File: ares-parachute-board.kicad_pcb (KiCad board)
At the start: 2 copper layers, 57 x 88 mm, 133 parts, among them J1 Conn_01x16_Female, J2 Conn_01x16_Female, J3 Conn_01x02_Male

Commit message: rename project
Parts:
- added U1: STM32F103CBTx, Package_QFP:LQFP-48_7x7mm_P0.5mm, F.Cu at (5.17, 5.17)
- added U2: LIS2DH, Package_LGA:LGA-14_2x2mm_P0.35mm_LayoutBorder3x4y, F.Cu at (1.32, 12.7)
- added U3: LIS2DH, Package_LGA:LGA-14_2x2mm_P0.35mm_LayoutBorder3x4y, F.Cu at (4.81, 12.7)

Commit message: re-annotate, component placement complete
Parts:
- added C10: 12.5p, Capacitor_SMD:C_0603_1608Metric, F.Cu at (189.6, 82.2)
- added C11: 100n, Capacitor_SMD:C_0603_1608Metric, F.Cu at (187.6, 67.8)
- added C12: 100n, Capacitor_SMD:C_0603_1608Metric, F.Cu at (197.0, 67.6)
- added C13: 100n, Capacitor_SMD:C_0603_1608Metric, F.Cu at (195.8, 78.6)
- added C14: 100n, Capacitor_SMD:C_0603_1608Metric, F.Cu at (185.6, 75.0)
- added C15: 4u7, Capacitor_SMD:C_0603_1608Metric, F.Cu at (187.0, 76.6)
- added C16: 100n, Capacitor_SMD:C_0603_1608Metric, F.Cu at (219.6, 83.0)
- added C17: 1F, asyd-parachute:SCMR18C105MRBA0, F.Cu at (196.0, 117.2)
- added C2: 1u, Capacitor_SMD:C_0603_1608Metric, F.Cu at (206.8, 62.6)
- added C3: 1u, Capacitor_SMD:C_0603_1608Metric, F.Cu at (200.0, 57.4)
- added C4: 10u, Capacitor_SMD:C_0603_1608Metric, F.Cu at (195.2, 61.6)
- added C5: 100n, Capacitor_SMD:C_0603_1608Metric, F.Cu at (196.8, 61.6)
- added C6: 47p, Capacitor_SMD:C_0603_1608Metric, F.Cu at (192.8, 61.8)
- added C7: 100n, Capacitor_SMD:C_0603_1608Metric, F.Cu at (205.0, 73.0)
- added C8: 12.5p, Capacitor_SMD:C_0603_1608Metric, F.Cu at (187.2, 82.2)
- added C9: 100n, Capacitor_SMD:C_0603_1608Metric, F.Cu at (204.2, 82.6)
- added J4: Conn_ARM_JTAG_SWD_10, Connector_PinHeader_1.27mm:PinHeader_2x05_P1.27mm_Vertical, F.Cu at (182.0, 67.8)
- added J5: Conn_01x03_Pin, Connector_PinHeader_2.54mm:PinHeader_1x03_P2.54mm_Horizontal, F.Cu at (226.2, 55.7)
- added J6: MPT 0.5/2-2.54, TerminalBlock_Phoenix:TerminalBlock_Phoenix_MPT-0,5-2-2.54_1x02_P2.54mm_Horizontal, F.Cu at (184.6, 101.1)
- added JP1: Jumper_3_Bridged12, Connector_PinHeader_2.54mm:PinHeader_1x03_P2.54mm_Horizontal, F.Cu at (191.6, 113.1)
- added LED1: RED, easyeda_exported:LED0805-R-RD, F.Cu at (199.4, 65.8)
- added LED2: RED, easyeda_exported:LED0805-R-RD, F.Cu at (214.2, 75.0)
- added LED3: YLW, easyeda_exported:LED0805-R-RD, F.Cu at (214.2, 72.4)
- added LED4: GRN, easyeda_exported:LED0805-R-RD, F.Cu at (214.2, 69.8)
- added R1: 33, Resistor_SMD:R_0603_1608Metric, F.Cu at (189.6, 61.8)
- added R10: 4k7, Resistor_SMD:R_0603_1608Metric, F.Cu at (217.2, 85.2)
- added R11: 4k7, Resistor_SMD:R_0603_1608Metric, F.Cu at (219.6, 87.4)
- added R12: 270, Resistor_SMD:R_0603_1608Metric, F.Cu at (210.4, 75.0)
- added R13: 270, Resistor_SMD:R_0603_1608Metric, F.Cu at (210.4, 72.4)
- added R14: 100, Resistor_SMD:R_0603_1608Metric, F.Cu at (210.4, 69.8)
- added R15: 100, Resistor_SMD:R_0603_1608Metric, F.Cu at (194.6, 106.8)
- added R2: 33, Resistor_SMD:R_0603_1608Metric, F.Cu at (191.2, 61.8)
- added R3: 270, Resistor_SMD:R_0603_1608Metric, F.Cu at (201.4, 65.2)
- added R4: 56k, Resistor_SMD:R_0603_1608Metric, F.Cu at (198.2, 57.4)
- added R5: 5.1k, Resistor_SMD:R_0603_1608Metric, F.Cu at (195.8, 55.0)
- added R6: 5.1k, Resistor_SMD:R_0603_1608Metric, F.Cu at (195.8, 58.2)
- added R7: 4k7, Resistor_SMD:R_0603_1608Metric, F.Cu at (201.8, 85.0)
- added R8: 4k7, Resistor_SMD:R_0603_1608Metric, F.Cu at (204.2, 87.2)
- added R9: 0, Resistor_SMD:R_0603_1608Metric, F.Cu at (193.4, 79.6)
- added U3: SR05-ES, Package_TO_SOT_SMD:SOT-143, F.Cu at (182.8, 56.8)
- added U4: W25Q128JVSIQTR, easyeda_exported:SOIC-8_L5.3-W5.3-P1.27-LS8.0-BL, F.Cu at (201.4, 73.0)
- added U6: STM32F103CBTx, Package_QFP:LQFP-48_7x7mm_P0.5mm, F.Cu at (192.4, 72.4)
- added U7: LIS2DW12TR, easyeda_exported:LGA-12_L2.0-W2.0-P0.50-BL, F.Cu at (219.7, 85.2)
- added USB1: TYPE-C16PIN, easyeda_exported:USB-C-SMD_TYPE-C16PIN, F.Cu at (189.8, 57.1)
- added X1: CSTNE8M00G520000R0, easyeda_exported:OSC-SMD_3P-L3.2-W1.3-P1.20, F.Cu at (191.6, 79.6)
- added X2: Q13FC1350000400, easyeda_exported:FC-135R_L3.2-W1.5, F.Cu at (188.4, 79.4)
- C1: value 1F -> 47p; footprint asyd-parachute:SCMR18C105MRBA0 -> Capacitor_SMD:C_0603_1608Metric
- U1: value STM32F103CBTx -> XC6206P332MR; footprint Package_QFP:LQFP-48_7x7mm_P0.5mm -> easyeda_exported:SOT-23-3_L2.9-W1.6-P1.90-LS2.8-BR
- U2: value LIS2DH -> AP2552W6-7; footprint Package_LGA:LGA-14_2x2mm_P0.35mm_LayoutBorder3x4y -> easyeda_exported:SOT-26_L3.0-W1.6-P0.95-LS2.8-BL
- U5: renamed from U3; value LIS2DH -> LIS2DW12TR; footprint Package_LGA:LGA-14_2x2mm_P0.35mm_LayoutBorder3x4y -> easyeda_exported:LGA-12_L2.0-W2.0-P0.50-BL
- moved U5 212.1 mm to (204.2, 85.0)
- moved U1 206.9 mm to (204.0, 62.4), turned to 90 degrees
- moved U2 204.8 mm to (200.4, 60.8), turned to -90 degrees
- moved C1 53.7 mm to (188.0, 61.8)
- moved REF** 27.8 mm to (184.6, 130.2)
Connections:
- net P0 renamed /DET+
- net P1 renamed /DET-
- net P13 renamed /PB9
- net P14 renamed /PB12
- net P15 renamed /PB13
- net P16 renamed /PB14
- net P19 renamed /PB15
- net P2 renamed /PB0
- net P20 renamed /PA3
- net P8 renamed /PB5
- net P9 renamed /PB8
- net btn_a renamed /PB1
- net btn_b renamed /PB2
- C1 pad 1: +3V3 -> /USB_D+
- J1 pad 1: +3V3 -> +3.3V
- J1 pad 3: MOT- -> +5V
- J2 pad 1: +3V3 -> +3.3V
- J2 pad 3: MOT- -> +5V
- U1 pad 1: unconnected-(U1-VBAT-Pad1) -> GND
- U1 pad 2: unconnected-(U1-PC13-Pad2) -> +5V
- U1 pad 3: unconnected-(U1-PC14-Pad3) -> +3.3V
- U2 pad 1: unconnected-(U2-SCL/SPC-Pad1) -> VBUS
- U2 pad 2: unconnected-(U2-SDA/SDI-Pad2) -> GND
- U2 pad 3: unconnected-(U2-SDO-Pad3) -> GND
- U2 pad 4: unconnected-(U2-~{CS}-Pad4) -> Net-(U2-~{FAULT})
- U2 pad 5: unconnected-(U2-INT2-Pad5) -> Net-(U2-ILIM)
- U2 pad 6: unconnected-(U2-INT1-Pad6) -> +5V
- U5 pad 1: unconnected-(U3-SCL/SPC-Pad1) -> /I2C1_SCL
- U5 pad 10: Net-(U3-GND-Pad10) -> +3.3V
- U5 pad 11: Net-(U3-GND-Pad10) -> unconnected-(U5-INT2-Pad11)
- U5 pad 12: Net-(U3-GND-Pad10) -> unconnected-(U5-INT1-Pad12)
- U5 pad 2: unconnected-(U3-SDA/SDI-Pad2) -> +3.3V
- U5 pad 3: unconnected-(U3-SDO-Pad3) -> GND
- U5 pad 4: unconnected-(U3-~{CS}-Pad4) -> /I2C1_SDA
- U5 pad 6: unconnected-(U3-INT1-Pad6) -> GND
- U5 pad 7: unconnected-(U3-Vdd_IO-Pad7) -> GND
- U5 pad 8: unconnected-(U3-Vdd-Pad8) -> GND
- U5 pad 9: Net-(U3-GND-Pad10) -> +3.3V
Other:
- board text added: "ARES Parachute Board PROTO1 (c) 2024 Hochschule Luzern, Technik & Architektur"
- board text added: "PA0"
- board text added: "PA1"
- board text added: "PA2"
- board text added: "Power Stuff"
- board text added: "X"
- board text added: "Y"
- board text added: "Z"
- board text added: "up"
- board text removed: "ASYD Parachute Board v1.3, SMD CONNECTOR (c) 2023 Hochschule Luzern, Technik & Architektur"

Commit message: about to try some stuff
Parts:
- removed J2: Conn_01x16_Female, Connector_PinHeader_2.54mm:PinHeader_1x16_P2.54mm_Vertical
- moved LED2 14.5 mm to (226.0, 66.5)
- moved R12 14.5 mm to (222.2, 66.5)
- moved LED3 12.3 mm to (226.0, 68.9)
- moved R13 12.3 mm to (222.2, 68.9)
- moved U4 12.3 mm to (213.2, 69.6)
- moved C7 12.3 mm to (216.8, 69.6)
- moved R14 11.9 mm to (222.2, 71.3)
- moved LED4 11.9 mm to (226.0, 71.3)
- moved C6 5.63 mm to (187.4, 63.4)
- moved J4 5.49 mm to (181.8, 62.4)
- moved C1 4.49 mm to (192.2, 63.4)
- moved R6 3.41 mm to (196.0, 54.8), turned to -90 degrees
- moved R5 3.01 mm to (196.0, 58.0), turned to 90 degrees
- moved R2 2.72 mm to (189.0, 63.4)
- moved R1 1.89 mm to (190.6, 63.4)
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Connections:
- net Net-(USB1-DN1) renamed /d-
- net Net-(USB1-DP1) renamed /d+
- J5 pad 1: /USART1_TX -> /USART1_RX
- J5 pad 2: /USART1_RX -> /USART1_TX
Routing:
- net +3.3V: track 0.00 -> 143.1 mm, vias 0 -> 4
- net +5V: track 0.00 -> 66.5 mm
- net /I2C1_SDA: track 0.00 -> 47.1 mm, vias 0 -> 2
- net /I2C2_SDA: track 0.00 -> 45.6 mm, vias 0 -> 4
- net /I2C1_SCL: track 0.00 -> 43.1 mm, vias 0 -> 2
- net /USART1_RX: track 0.00 -> 40.1 mm, vias 0 -> 2
- net /PB8: track 0.00 -> 39.9 mm, vias 0 -> 1
- net /PB5: track 0.00 -> 39.4 mm, vias 0 -> 2
- net /PB9: track 0.00 -> 39.4 mm, vias 0 -> 1
- net /USART1_TX: track 0.00 -> 38.6 mm, vias 0 -> 2
- net /I2C2_SCL: track 0.00 -> 37.1 mm, vias 0 -> 4
- net /RED: track 0.00 -> 37.1 mm, vias 0 -> 4
- net /YLW: track 0.00 -> 34.7 mm, vias 0 -> 4
- net VBUS: track 0.00 -> 34.0 mm, vias 0 -> 2
- net /GRN: track 0.00 -> 32.0 mm, vias 0 -> 4
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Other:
- outline, holes or cut-outs redrawn

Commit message: layout done
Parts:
- removed the   at (228.6, 133.3)
- added  : , asyd-parachute:my_pin, F.Cu at (205.4, 124.8)
- added  : , asyd-parachute:my_pin, F.Cu at (207.9, 129.8)
- added  : , asyd-parachute:my_pin, F.Cu at (207.9, 132.4)
- added  : , asyd-parachute:my_pin, F.Cu at (205.4, 112.1)
- added  : , asyd-parachute:my_pin, F.Cu at (210.5, 127.3)
- added  : , asyd-parachute:my_pin, F.Cu at (207.9, 117.1)
- added  : , asyd-parachute:my_pin, F.Cu at (207.9, 119.7)
- added  : , asyd-parachute:my_pin, F.Cu at (205.4, 109.5)
- added  : , asyd-parachute:my_pin, F.Cu at (207.9, 109.5)
- added  : , asyd-parachute:my_pin, F.Cu at (210.5, 119.7)
- added  : , asyd-parachute:my_pin, F.Cu at (207.9, 137.5)
- added  : , asyd-parachute:my_pin, F.Cu at (205.4, 122.2)
- added  : , asyd-parachute:my_pin, F.Cu at (207.9, 112.1)
- added  : , asyd-parachute:my_pin, F.Cu at (210.5, 117.1)
- added  : , asyd-parachute:my_pin, F.Cu at (210.5, 114.6)
- added  : , asyd-parachute:my_pin, F.Cu at (205.4, 129.8)
- added  : , asyd-parachute:my_pin, F.Cu at (205.4, 127.3)
- added  : , asyd-parachute:my_pin, F.Cu at (210.5, 122.2)
- added  : , asyd-parachute:my_pin, F.Cu at (210.5, 132.4)
- added  : , asyd-parachute:my_pin, F.Cu at (210.5, 107.0)
- added  : , asyd-parachute:my_pin, F.Cu at (205.4, 107.0)
- added  : , asyd-parachute:my_pin, F.Cu at (210.5, 109.5)
- added  : , asyd-parachute:my_pin, F.Cu at (210.5, 124.8)
- added  : , asyd-parachute:my_pin, F.Cu at (205.4, 134.9)
- added  : , asyd-parachute:my_pin, F.Cu at (210.5, 104.4)
- added  : , asyd-parachute:my_pin, F.Cu at (205.4, 114.6)
- added  : , asyd-parachute:my_pin, F.Cu at (207.9, 122.2)
- added  : , asyd-parachute:my_pin, F.Cu at (205.4, 119.7)
- added  : , asyd-parachute:my_pin, F.Cu at (207.9, 124.8)
- added  : , asyd-parachute:my_pin, F.Cu at (210.5, 137.5)
- added  : , asyd-parachute:my_pin, F.Cu at (205.4, 104.4)
- added  : , asyd-parachute:my_pin, F.Cu at (205.4, 132.4)
- added  : , asyd-parachute:my_pin, F.Cu at (210.5, 129.8)
- added  : , asyd-parachute:my_pin, F.Cu at (205.4, 117.1)
- added  : , asyd-parachute:my_pin, F.Cu at (207.9, 107.0)
- added  : , asyd-parachute:my_pin, F.Cu at (210.5, 112.1)
- added  : , asyd-parachute:my_pin, F.Cu at (205.4, 137.5)
- added  : , asyd-parachute:my_pin, F.Cu at (207.9, 104.4)
- added  : , asyd-parachute:my_pin, F.Cu at (207.9, 134.9)
- added  : , asyd-parachute:my_pin, F.Cu at (207.9, 114.6)
- added  : , asyd-parachute:my_pin, F.Cu at (210.5, 134.9)
- added  : , asyd-parachute:my_pin, F.Cu at (207.9, 127.3)
- added REF**: MountingHole_2.2mm_M2, MountingHole:MountingHole_2.2mm_M2, F.Cu at (182.3, 97.4)
- added REF**: MountingHole_2.2mm_M2, MountingHole:MountingHole_2.2mm_M2, F.Cu at (234.8, 75.2)
- added REF**: MountingHole_2.2mm_M2, MountingHole:MountingHole_2.2mm_M2, F.Cu at (234.2, 137.4)
- added REF**: MountingHole_2.2mm_M2, MountingHole:MountingHole_2.2mm_M2, F.Cu at (190.0, 97.1)
- added REF**: MountingHole_2.2mm_M2, MountingHole:MountingHole_2.2mm_M2, F.Cu at (234.7, 83.6)
- added REF**: MountingHole_2.2mm_M2, MountingHole:MountingHole_2.2mm_M2, F.Cu at (184.6, 83.5)
- added REF**: MountingHole_2.2mm_M2, MountingHole:MountingHole_2.2mm_M2, F.Cu at (202.6, 137.4)
- moved R15 9.90 mm to (190.7, 115.9), turned to 0 degrees
- moved J1 6.35 mm to (195.6, 98.0), turned to 90 degrees
- moved   6.27 mm to (225.7, 134.9)
- moved   6.27 mm to (225.7, 137.5)
- moved   6.27 mm to (225.7, 109.5)
- moved   6.27 mm to (225.7, 114.6)
- moved   6.27 mm to (225.7, 117.1)
- moved   6.27 mm to (225.7, 104.4)
- moved   6.27 mm to (225.7, 119.7)
- moved   6.27 mm to (225.7, 122.2)
- moved   6.27 mm to (225.7, 127.3)
- moved   6.27 mm to (225.7, 107.0)
- moved   6.27 mm to (225.7, 112.1)
- moved   6.27 mm to (225.7, 124.8)
- moved   6.27 mm to (225.7, 129.8)
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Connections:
- J1 pad 1: +3.3V -> +5V
- J1 pad 10: /PB8 -> /PB1
- J1 pad 11: /PB9 -> /PB2
- J1 pad 12: /PB12 -> /PB15
- J1 pad 13: /PB13 -> /PB14
- J1 pad 14: /PB14 -> /PB13
- J1 pad 15: /PB15 -> /PB12
- J1 pad 16: /PA3 -> unconnected-(J1-Pin_16-Pad16)
- J1 pad 2: GND -> +3.3V
- J1 pad 3: +5V -> GND
- J1 pad 6: /PB0 -> /PB5
- J1 pad 7: /PB1 -> /PB8
- J1 pad 8: /PB2 -> /PB9
- J1 pad 9: /PB5 -> /PB0
- JP1 pad 1: +5V -> Net-(JP1-A)
- JP1 pad 3: Net-(JP1-B) -> +5V
- R15 pad 2: Net-(JP1-B) -> Net-(JP1-A)
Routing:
- net /PB12: track 1.78 -> 59.2 mm, vias 1 -> 5
- net /PB13: track 2.15 -> 57.4 mm, vias 1 -> 5
- net /PB14: track 2.07 -> 55.7 mm, vias 1 -> 5
- net /PB15: track 1.21 -> 52.8 mm, vias 1 -> 5
- net /PB2: track 0.00 -> 42.7 mm, vias 0 -> 2
- net /PB1: track 0.00 -> 41.3 mm, vias 0 -> 2
- net /PB0: track 0.00 -> 40.0 mm, vias 0 -> 2
- net /PB9: track 39.4 -> 56.5 mm, vias 1 -> 2
- net /PB8: track 39.9 -> 55.4 mm, vias 1 -> 2
- net /PB5: track 39.4 -> 53.9 mm
- net +5V: track 66.5 -> 60.0 mm, vias 0 -> 2
- net +3.3V: track 143.1 -> 149.5 mm, vias 4 -> 6
- net Net-(JP1-B): track 3.20 -> 0.00 mm
- net GND: track 13.6 -> 16.6 mm, vias 23 -> 32
- net Net-(JP1-A): track 0.00 -> 2.80 mm
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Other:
- outline, holes or cut-outs redrawn
- board text added: "3V3"
- board text added: "5V"
- board text added: "DET+"
- board text added: "DET-"
- board text added: "GND"
- board text added: "I2C1"
- board text added: "I2C2"
- board text added: "One Accelerometer can break!"
- board text added: "PB0"
- board text added: "PB1"
- board text added: "PB12"
- board text added: "PB13"
- board text added: "PB14"
- board text added: "PB15"
- board text added: "PB2"
- board text added: "PB5"
- board text added: "PB8"
- board text added: "PB9"
- board text added: "RX"
- board text added: "SAFE SIDE"
- board text added: "SPI1"
- board text added: "TX"
- board text added: "UNSAFE SIDE"
- board text added: "USART1"

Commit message: added testpoints, not on board yet
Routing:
- net /PB13: track 57.4 -> 55.3 mm, vias 5 -> 4
- net /PB14: track 55.7 -> 53.6 mm, vias 5 -> 4
- net /PB12: track 59.2 -> 57.4 mm, vias 5 -> 4
- net /PB15: track 52.8 -> 51.6 mm, vias 5 -> 4
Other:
- board text added: "SAFE AREA"
- board text added: "UNSAFE AREA"
- board text added: "UNSAFE AREA Pins below are safe"
- board text removed: "SAFE SIDE"
- board text removed: "UNSAFE SIDE"

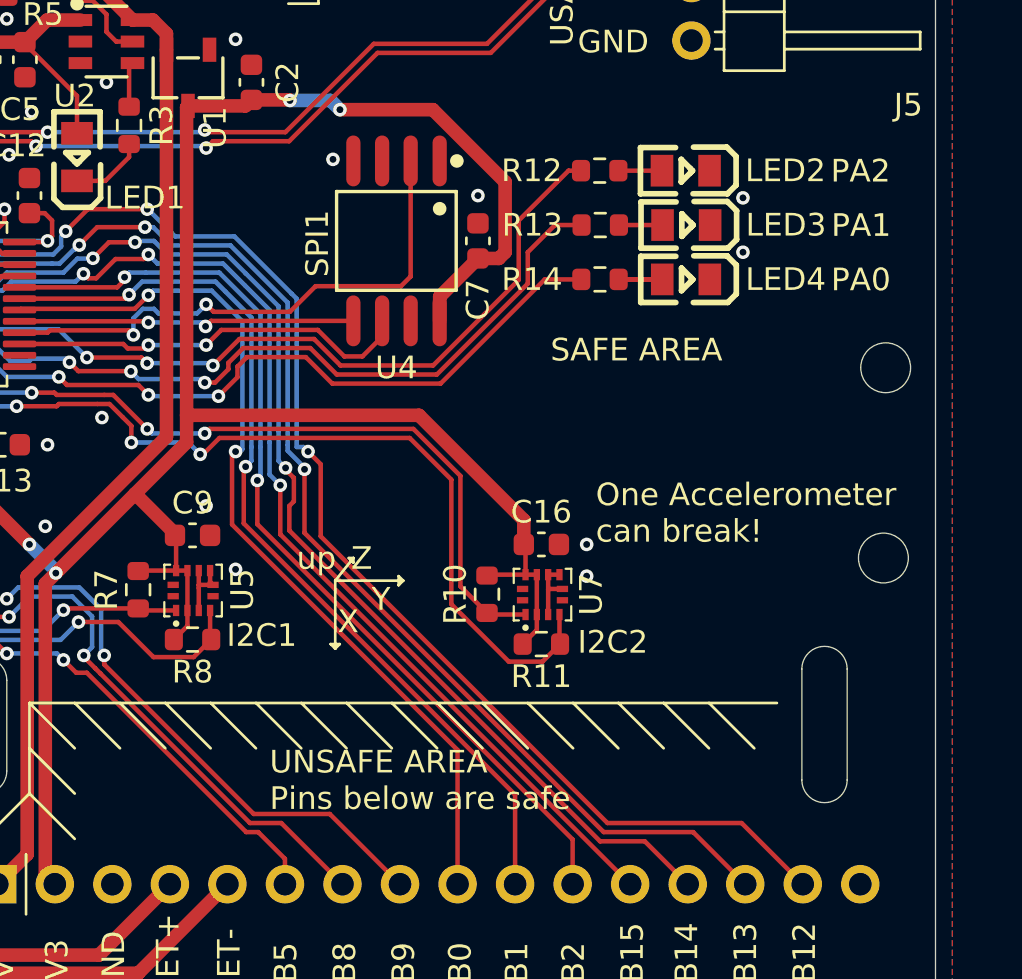
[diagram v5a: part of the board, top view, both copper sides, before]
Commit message: added testpoints
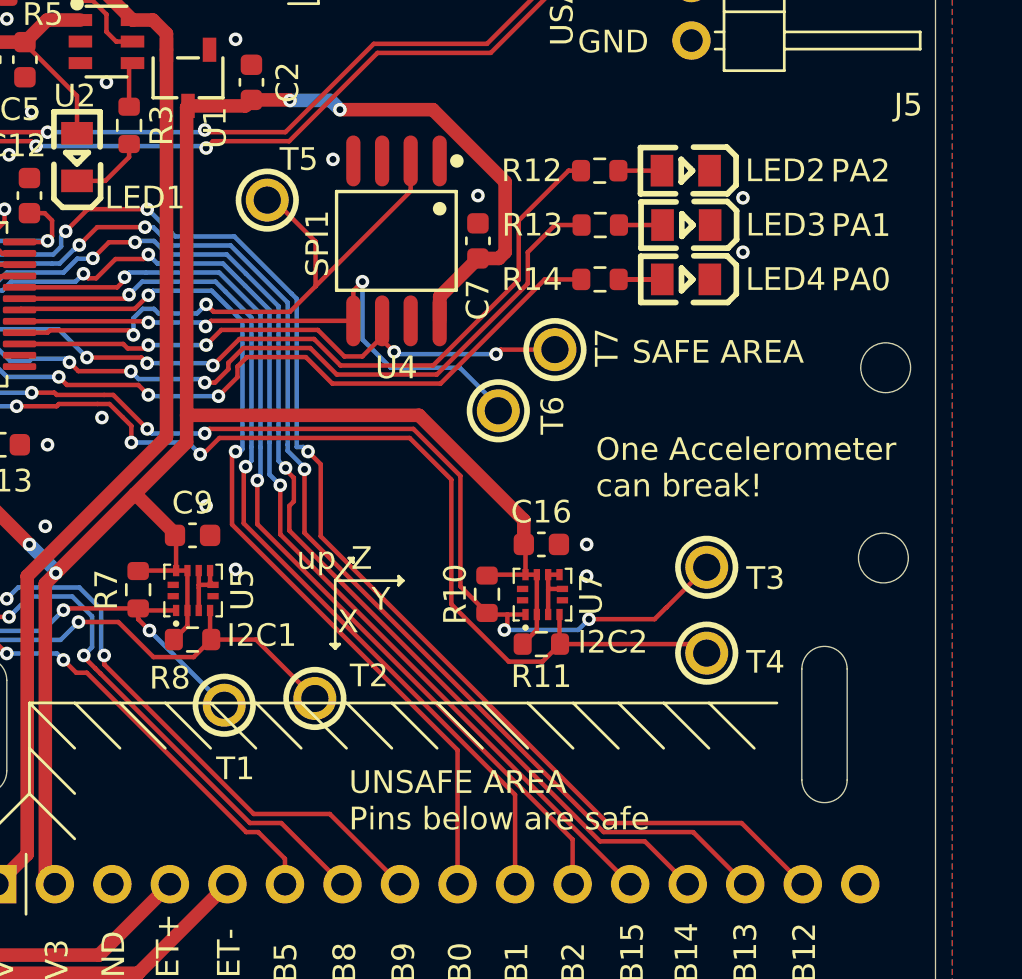
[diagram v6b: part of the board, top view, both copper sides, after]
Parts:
- added T1: RH-5000, easyeda_exported:TEST-TH_BD2.54-P1.4_RED, F.Cu at (205.6, 90.1)
- added T2: RH-5000, easyeda_exported:TEST-TH_BD2.54-P1.4_RED, F.Cu at (209.6, 89.8)
- added T3: RH-5000, easyeda_exported:TEST-TH_BD2.54-P1.4_RED, F.Cu at (226.9, 84.0)
- added T4: RH-5000, easyeda_exported:TEST-TH_BD2.54-P1.4_RED, F.Cu at (226.9, 87.8)
- added T5: RH-5000, easyeda_exported:TEST-TH_BD2.54-P1.4_RED, F.Cu at (207.5, 67.8)
- added T6: RH-5000, easyeda_exported:TEST-TH_BD2.54-P1.4_RED, F.Cu at (217.7, 77.1)
- added T7: RH-5000, easyeda_exported:TEST-TH_BD2.54-P1.4_RED, F.Cu at (220.2, 74.4)
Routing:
- net /SPI1_MOSI: track 14.9 -> 26.8 mm, vias 2 -> 3
- net /I2C2_SCL: track 38.8 -> 49.7 mm, vias 4 -> 6
- net /SPI1_SCK: track 18.0 -> 26.8 mm, vias 2 -> 4
- net /I2C2_SDA: track 45.6 -> 52.2 mm
- net /I2C1_SCL: track 43.1 -> 49.0 mm, vias 2 -> 3
- net /I2C1_SDA: track 47.0 -> 52.7 mm
- net /SPI1_MISO: track 24.4 -> 27.1 mm
